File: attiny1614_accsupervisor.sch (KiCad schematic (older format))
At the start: 5 parts

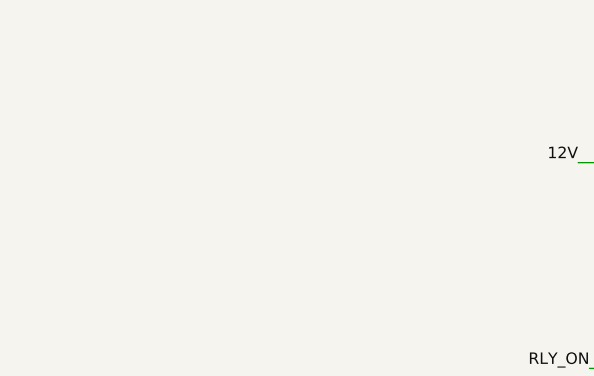
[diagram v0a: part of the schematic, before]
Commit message: VXO7803 library added
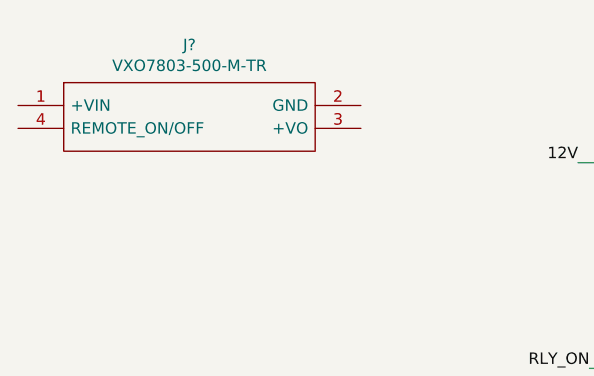
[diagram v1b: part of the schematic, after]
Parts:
- added J?: VXO7803-500-M-TR, SamacSys_Parts:VXO7803500MTR, symbol SamacSys_Parts:VXO7803-500-M-TR
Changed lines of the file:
@@
+	1    0    0    -1
+$EndComp
+$Comp
+L SamacSys_Parts:VXO7803-500-M-TR J?
+U 1 1 5F4CCD41
+P 1100 1700
+F 0 "J?" H 1850 1965 50  0000 C CNN
+F 1 "VXO7803-500-M-TR" H 1850 1874 50  0000 C CNN
+F 2 "SamacSys_Parts:VXO7803500MTR" H 2450 1800 50  0001 L CNN
+F 3 "https://www.mouser.ch/datasheet/2/670/vxo78-500-m-1729064.pdf" H 2450 1700 50  0001 L CNN
+F 4 "Non-Isolated DC/DC Converters dc-dc non-isolated, 0.5 A, 4.75~36 Vdc input, 3.3 Vdc output, SMT, open frame, tape and reel" H 2450 1600 50  0001 L CNN "Description"
+F 5 "3.5" H 2450 1500 50  0001 L CNN "Height"
+F 6 "490-VXO7803-500-M-TR" H 2450 1400 50  0001 L CNN "Mouser Part Number"
+F 7 "https://www.mouser.co.uk/ProductDetail/CUI-Inc/VXO7803-500-M-TR?qs=GBLSl2AkiruqsgUrpmz5tw%3D%3D" H 2450 1300 50  0001 L CNN "Mouser Price/Stock"
+F 8 "CUI Inc" H 2450 1200 50  0001 L CNN "Manufacturer_Name"
+F 9 "VXO7803-500-M-TR" H 2450 1100 50  0001 L CNN "Manufacturer_Part_Number"
+	1    1100 1700
 	1    0    0    -1
 $EndComp

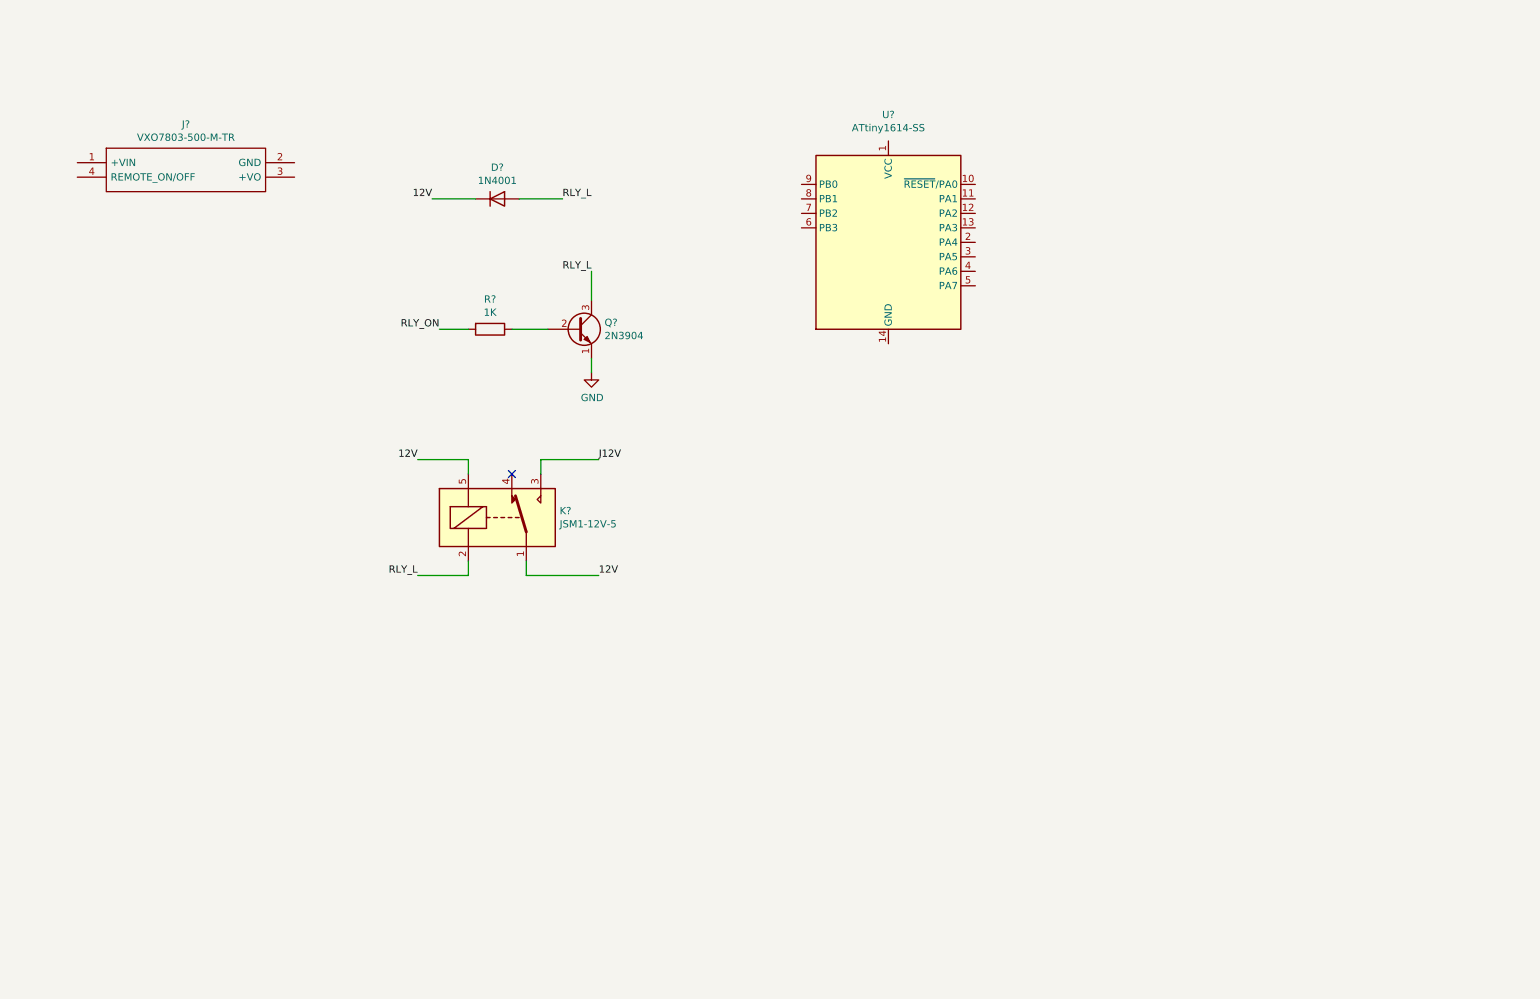
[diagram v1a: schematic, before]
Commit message: UPDI, JST hdrs added
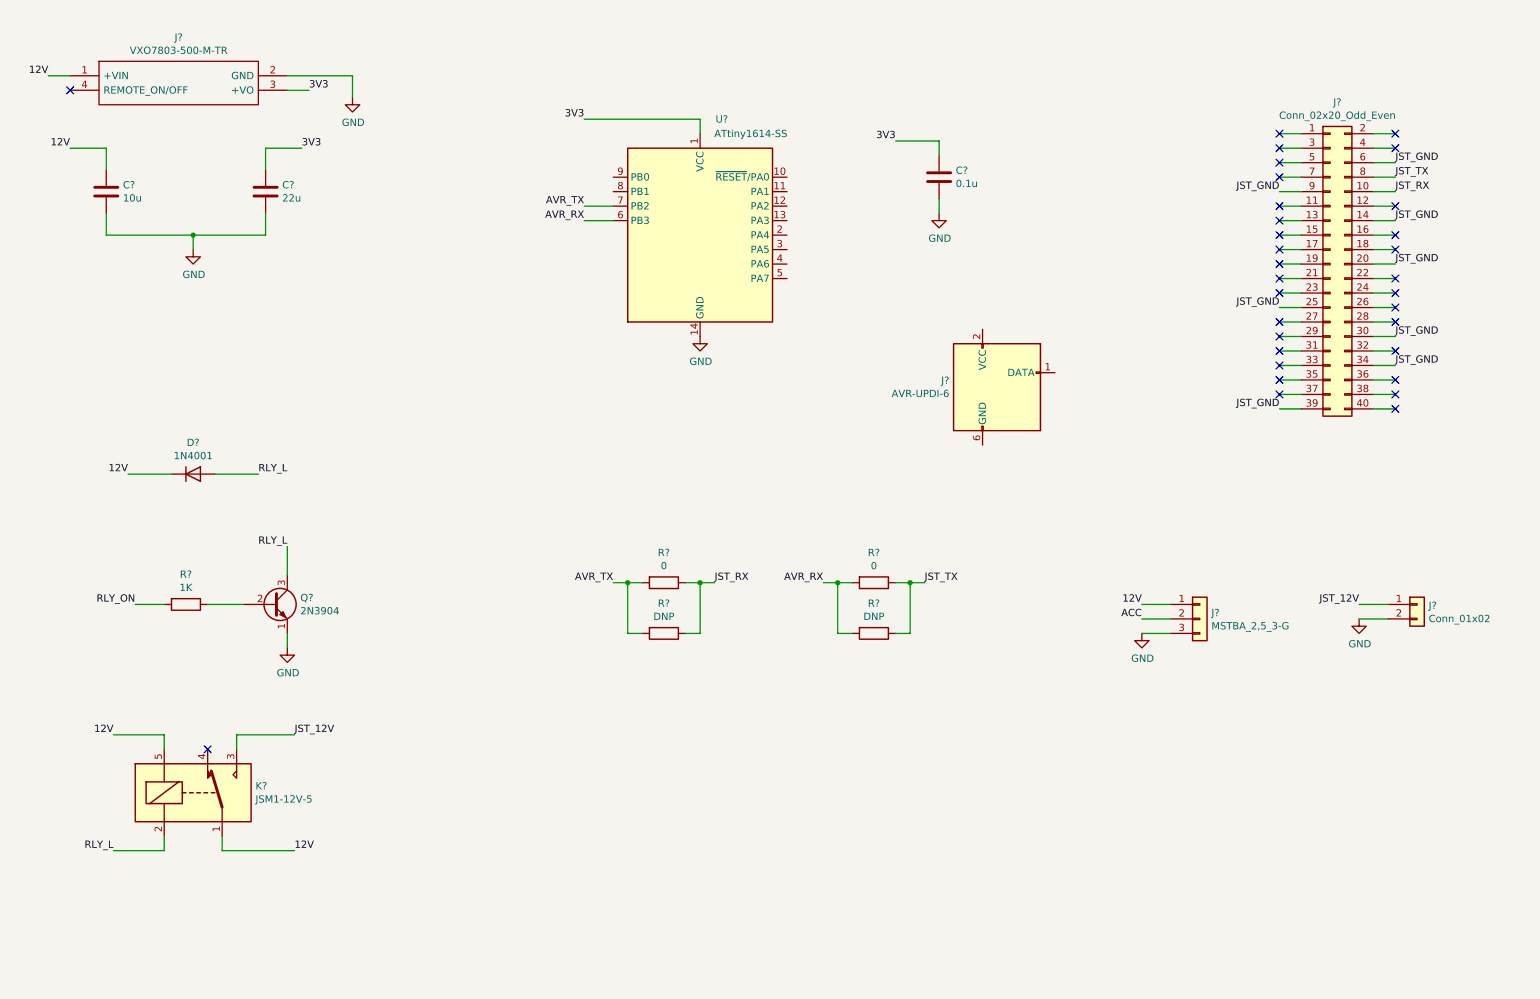
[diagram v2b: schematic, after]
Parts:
- added C?: 0.1u, Capacitor_SMD:C_1206_3216Metric_Pad1.42x1.75mm_HandSolder, symbol Device:C
- added C?: 10u, symbol Device:C
- added C?: 22u, symbol Device:C
- added J?: Conn_02x20_Odd_Even, symbol Connector_Generic:Conn_02x20_Odd_Even
- added J?: MSTBA_2,5_3-G, Connector_Phoenix_MSTB:PhoenixContact_MSTBA_2,5_3-G_1x03_P5.00mm_Horizontal, symbol Connector_Generic:Conn_01x03
- added J?: Conn_01x02, TerminalBlock_Phoenix:TerminalBlock_Phoenix_PT-1,5-2-5.0-H_1x02_P5.00mm_Horizontal, symbol Connector_Generic:Conn_01x02
- added J?: AVR-UPDI-6, Connector_PinHeader_2.54mm:PinHeader_2x03_P2.54mm_Vertical, symbol Connector:AVR-UPDI-6
- added R? (x2): 0, symbol Device:R
- added R? (x2): DNP, symbol Device:R
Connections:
- net 12V: now also J?.1 (+VIN), C?.1, J?.1 (Pin_1)
- net GND: now also J?.2 (GND), U?.14 (GND), C?.2, C?.2, C?.2, J?.2 (Pin_2), J?.3 (Pin_3)
- net 3V3: now reaches U?.1 (VCC)
- net 3V3: now also J?.3 (+VO), C?.1, C?.1
- net AVR_RX: now reaches U?.6 (PB3)
- net AVR_RX: now also R?.2, R?.2
- net AVR_TX: now reaches U?.7 (PB2)
- net AVR_TX: now also R?.2, R?.2
- net J12V renamed JST_12V
- net JST_12V: now also J?.1 (Pin_1)
- new net ACC: J?.2 (Pin_2)
- new net JST_GND: J?.14 (Pin_14), J?.20 (Pin_20), J?.25 (Pin_25), J?.30 (Pin_30), J?.34 (Pin_34), J?.39 (Pin_39), J?.6 (Pin_6), J?.9 (Pin_9)
- new net JST_RX: J?.10 (Pin_10), R?.1, R?.1
- new net JST_TX: J?.8 (Pin_8), R?.1, R?.1
- no-connect marks 1 -> 32
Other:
- moved on the sheet: D?, J?, K?, Q?, R?, U?

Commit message: Netlist generated
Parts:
- removed D?: 1N4001, Diode_THT:D_DO-41_SOD81_P10.16mm_Horizontal, symbol Diode:1N4001
- removed Q?: 2N3904, Package_TO_SOT_THT:TO-92_Inline, symbol Transistor_BJT:2N3904
- added D1: US1A, Diode_SMD:D_SMA, symbol Diode:US1A
- added F1: 10A, attiny1614_accsupervisor:Fuseholder_Cylinder-5x20mm_Geoyoung_GF-205B, symbol Device:Fuse
- added F2: 2A, attiny1614_accsupervisor:Fuseholder_Cylinder-5x20mm_Geoyoung_GF-205B, symbol Device:Fuse
- added Q1, Q2, Q3: BC817, Package_TO_SOT_SMD:SOT-23, symbol Transistor_BJT:BC817
- added Q4, Q5: BSS84, Package_TO_SOT_SMD:SOT-23, symbol Transistor_FET:BSS84
- added R10, R11: 2.2k, Resistor_SMD:R_1206_3216Metric_Pad1.42x1.75mm_HandSolder, symbol Device:R
- added R2, R3: 1k, Resistor_SMD:R_1206_3216Metric_Pad1.42x1.75mm_HandSolder, symbol Device:R
- added R4, R5, R8, R9: 10k, Resistor_SMD:R_1206_3216Metric_Pad1.42x1.75mm_HandSolder, symbol Device:R
- added R6, R7: DNP, Resistor_SMD:R_1206_3216Metric_Pad1.42x1.75mm_HandSolder, symbol Device:R
- C1, C2: renamed from C?; footprint (none) -> Capacitor_SMD:C_1206_3216Metric_Pad1.42x1.75mm_HandSolder
- J4: renamed from J?; footprint (none) -> Connector_PinHeader_2.54mm:PinHeader_2x20_P2.54mm_Vertical
- R1, R12, R13, R14, R15: renamed from R?; footprint (none) -> Resistor_SMD:R_1206_3216Metric_Pad1.42x1.75mm_HandSolder
- gave numbers to parts that had none: 7
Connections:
- net JST_GND is gone; now on net GND: J4.14 (Pin_14), J4.20 (Pin_20), J4.25 (Pin_25), J4.30 (Pin_30), J4.34 (Pin_34), J4.39 (Pin_39), J4.6 (Pin_6), J4.9 (Pin_9)
- net 12V: now also D1.1 (K), F1.2, Q4.3 (D), R4.2, R6.2; no longer J2.1 (Pin_1)
- net 3V3: now also J5.2 (VCC)
- net ACC: now also F2.2, Q5.3 (D), R5.2, R7.2; no longer J2.2 (Pin_2)
- net GND: now also J5.6 (GND), Q1.2 (E), Q2.2 (E), Q3.2 (E), R10.1, R11.1
- net RLY_ON: now also U1.11 (PA1)
- net UPDI_DATA: now reaches U1.10 (~RESET~/PA0)
- net UPDI_DATA: now also J5.1 (DATA)
- net ADC1_VIN: now reaches U1.4 (PA6)
- net ADC1_VIN: now also R10.2, R8.1
- net ADC2_ACC: now reaches U1.5 (PA7)
- net ADC2_ACC: now also R11.2, R9.1
- net at R1.1: now also Q1.1 (B)
- net RLY_L: no longer names the net of K1.2
- net RLY_L: now also D1.2 (A), Q1.3 (C)
- new net: Q4.2 (S), R6.1, R8.2
- new net: Q2.1 (B), R2.1
- new net: Q2.3 (C), Q4.1 (G), R4.1
- new net: Q5.2 (S), R7.1, R9.2
- new net: Q3.1 (B), R3.1
- new net: Q3.3 (C), Q5.1 (G), R5.1
- new net 12V_IN: F1.1, J2.1 (Pin_1)
- new net ACC_IN: F2.1, J2.2 (Pin_2)
- new net ADC_ON: R2.2, R3.2
- no-connect marks 32 -> 38
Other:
- moved on the sheet: C1, C2, C3, J1, J2, J3, J4, J5, K1, R1, R12, R13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

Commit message: First layout
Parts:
- added H1: 3.2mm, MountingHole:MountingHole_3.2mm_M3, symbol Mechanical:MountingHole
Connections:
- net JST_RX: now also R15.1; no longer R13.1
- net JST_TX: now also R13.1; no longer R15.1
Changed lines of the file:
@@
 encoding utf-8
 Sheet 1 1
-Title ""
-Date ""
-Rev ""
+Title "ATTINY-ACC-Supervisor"
+Date "2020-09-01"
+Rev "r01"
 Comp ""
 Comment1 ""
 Comment2 ""
 Comment3 ""
-Comment4 ""
+Comment4 "(c) 2020, Jason Kwon"
 $EndDescr
 $Comp
@@
 Wire Wire Line
 	8500 1450 8400 1450
-Wire Wire Line
-	8900 1450 9000 1450
-Wire Wire Line
-	8900 1800 9000 1800
-Wire Wire Line
-	9000 1800 9000 1450
-Connection ~ 9000 1450
-Wire Wire Line
-	9000 1450 9100 1450
 Text Label 8400 1450 2    50   ~ 0
 AVR_TX
@@
 Wire Wire Line
 	8500 2250 8400 2250
-Wire Wire Line
-	8900 2250 9000 2250
-Wire Wire Line
-	8900 2600 9000 2600
-Wire Wire Line
-	9000 2600 9000 2250
-Connection ~ 9000 2250
-Wire Wire Line
-	9000 2250 9100 2250
 Text Label 8400 2250 2    50   ~ 0
 AVR_RX
@@
 	1    0    0    -1
 $EndComp
+$Comp
+L Mechanical:MountingHole H1
+U 1 1 5F7DB97A
+P 4200 6900
+F 0 "H1" H 4300 6946 50  0000 L CNN
+F 1 "3.2mm" H 4300 6855 50  0000 L CNN
+F 2 "MountingHole:MountingHole_3.2mm_M3" H 4200 6900 50  0001 C CNN
+F 3 "~" H 4200 6900 50  0001 C CNN
+	1    4200 6900
+	1    0    0    -1
+$EndComp
+$Comp
+L Graphic:Logo_Open_Hardware_Large #LOGO1
+U 1 1 5F7F496C
+P 5450 7050
+F 0 "#LOGO1" H 5450 7550 50  0001 C CNN
+F 1 "Logo_Open_Hardware_Large" H 5450 6650 50  0001 C CNN
+F 2 "attiny1614_accsupervisor:Doge" H 5450 7050 50  0001 C CNN
+F 3 "~" H 5450 7050 50  0001 C CNN
+	1    5450 7050
+	1    0    0    -1
+$EndComp
+Wire Wire Line
+	8900 1450 9100 1450
+Text Label 9100 1800 0    50   ~ 0
+JST_TX
+Wire Wire Line
+	8900 1800 9100 1800
+Wire Wire Line
+	8900 2250 9100 2250
+Text Label 9100 2600 0    50   ~ 0
+JST_RX
+Wire Wire Line
+	8900 2600 9100 2600
 $EndSCHEMATC

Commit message: r01 gerber generated
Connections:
- net ADC1_VIN: now also U1.5 (PA7); no longer U1.4 (PA6)
- net ADC2_ACC: now also U1.4 (PA6); no longer U1.5 (PA7)
- net ADC_ON: now also U1.12 (PA2)
- no-connect marks 38 -> 37
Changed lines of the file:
@@
 	6250 1750 6450 1750
 Text Label 6450 1750 0    50   ~ 0
-ADC1_VIN
+ADC2_ACC
 Wire Wire Line
 	6250 1850 6450 1850
 Text Label 6450 1850 0    50   ~ 0
-ADC2_ACC
+ADC1_VIN
 NoConn ~ 5050 1150
 NoConn ~ 5050 1250
-NoConn ~ 6250 1350
 NoConn ~ 6250 1450
 NoConn ~ 6250 1550
@@
 Wire Wire Line
 	8900 2600 9100 2600
+Wire Wire Line
+	6250 1350 6450 1350
+Text Label 6450 1350 0    50   ~ 0
+ADC_ON
 $EndSCHEMATC

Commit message: Layout done
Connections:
- net ADC1_VIN: now also U1.11 (PA1); no longer U1.5 (PA7)
- net ADC2_ACC: now also U1.12 (PA2); no longer U1.4 (PA6)
- net ADC_ON: now also U1.13 (PA3); no longer U1.12 (PA2)
- net RLY_ON: now also U1.8 (PB1); no longer U1.11 (PA1)
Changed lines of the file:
@@
 UPDI_DATA
 Wire Wire Line
+	5050 1250 4850 1250
+Text Label 4850 1250 2    50   ~ 0
+RLY_ON
+Wire Wire Line
 	6250 1250 6450 1250
+Text Label 6450 1350 0    50   ~ 0
+ADC2_ACC
+Wire Wire Line
+	6250 1350 6450 1350
 Text Label 6450 1250 0    50   ~ 0
-RLY_ON
-Wire Wire Line
-	6250 1750 6450 1750
-Text Label 6450 1750 0    50   ~ 0
-ADC2_ACC
-Wire Wire Line
-	6250 1850 6450 1850
-Text Label 6450 1850 0    50   ~ 0
 ADC1_VIN
 NoConn ~ 5050 1150
-NoConn ~ 5050 1250
-NoConn ~ 6250 1450
 NoConn ~ 6250 1550
 NoConn ~ 6250 1650
@@
 	8900 2600 9100 2600
 Wire Wire Line
-	6250 1350 6450 1350
-Text Label 6450 1350 0    50   ~ 0
+	6250 1450 6450 1450
+Text Label 6450 1450 0    50   ~ 0
 ADC_ON
+NoConn ~ 6250 1750
+NoConn ~ 6250 1850
 $EndSCHEMATC
